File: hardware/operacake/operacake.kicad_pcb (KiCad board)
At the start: 4 copper layers, 120 x 75 mm, 152 parts, among them J1 CONN_02X20, J2 CONN_02X20, P1 ADDRESS, P20 GPIO, P22 I2S, P28 SD, P9 BASEBAND, U1 MASWSS0129, U10 74LVC1G58, U11 74LVC1G58, U12 74LVC1G58, U13 74LVC1G58, U14 74AHC1G02, U15 74AHC1G02, U16 74LVC1G19, U2 SKY13322, U3 SKY13322, U4 PCA9557, U5 TC7MBL3245CFT, U6 74LVC1G58, U7 74LVC1G58, U8 74AHC1G08, U9 74AHC1G08

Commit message: Sync reviewing of hardware
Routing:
- added copper zone on In1.Cu, net GND
- added copper zone on In2.Cu, net VCC
- removed copper zone on C2, net GND
- removed copper zone on C3, net VCC
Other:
- net class Default removed

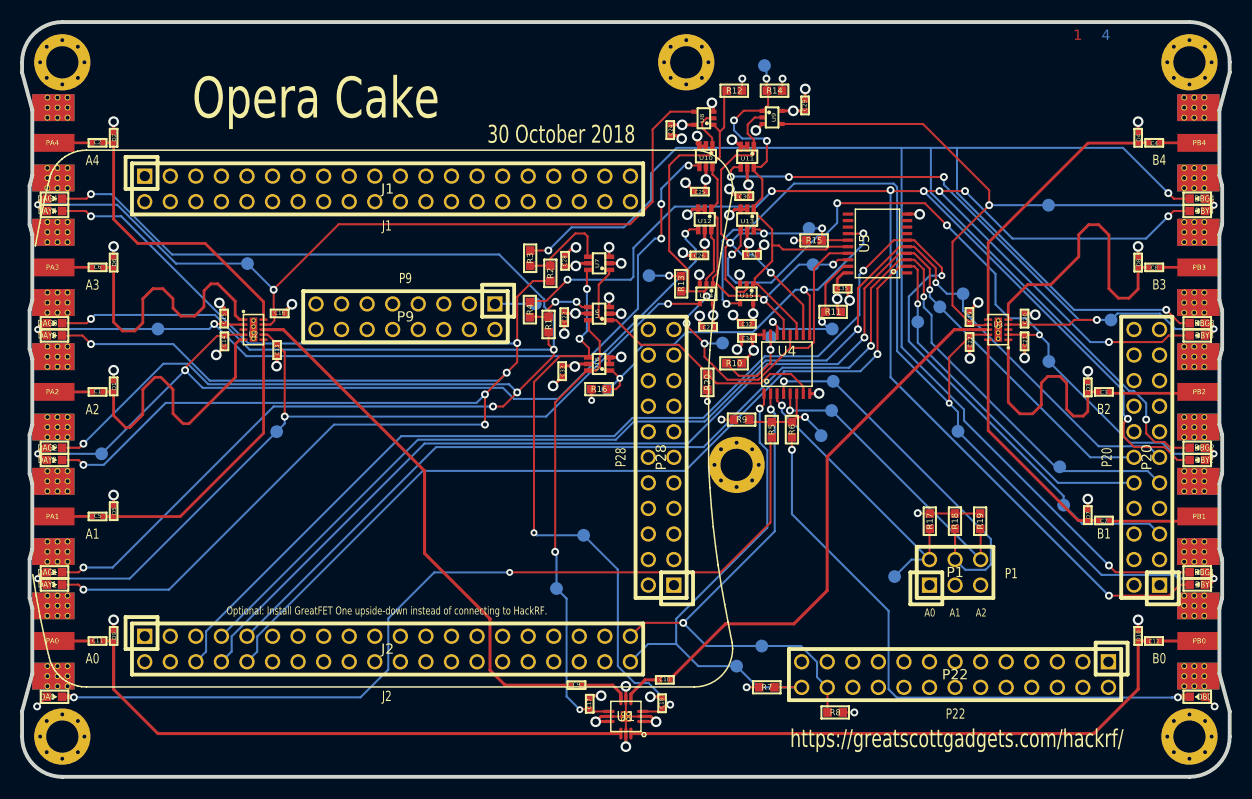
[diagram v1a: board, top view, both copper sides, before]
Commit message: Revert "Sync reviewing of hardware"
This reverts commit 25548c0c8d53f1e9841cca2a1484c655ffdb1925.
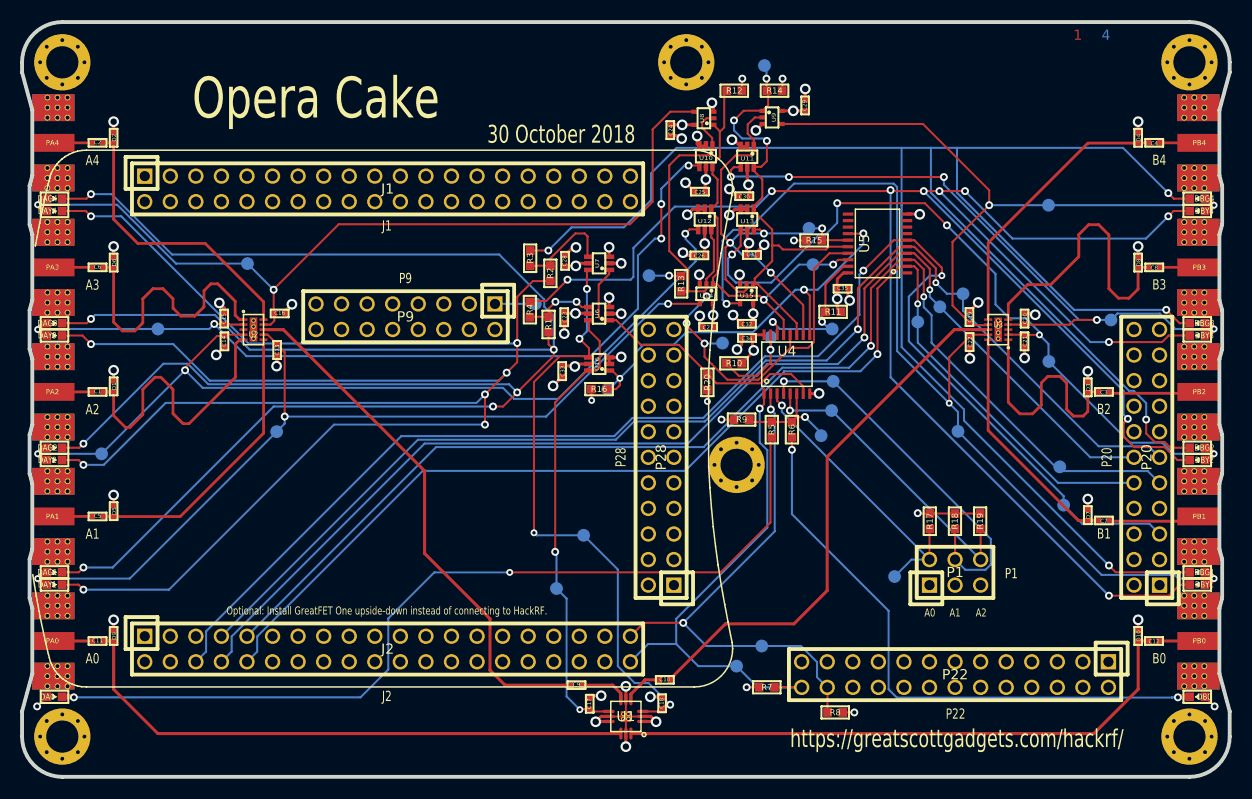
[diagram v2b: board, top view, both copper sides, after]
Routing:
- added copper zone on C2, net GND
- added copper zone on C3, net VCC
- removed copper zone on In1.Cu, net GND
- removed copper zone on In2.Cu, net VCC
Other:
- net class Default added: clearance 0.1524, trace_width 0.2794, via_dia 0.6858, via_drill 0.3302
